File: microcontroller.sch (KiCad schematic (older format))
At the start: 52 parts, among them J3 FH12A-10S-0.5SH55, J4 , J5 Conn_ARM_JTAG_SWD_20, J6 26642801RP2, SW0 SW_Push, SW1 SW_Push, SW2 SW_Push, SW3 SW_Push, SW6 SW_Push, U7 EFM32GG942F1024

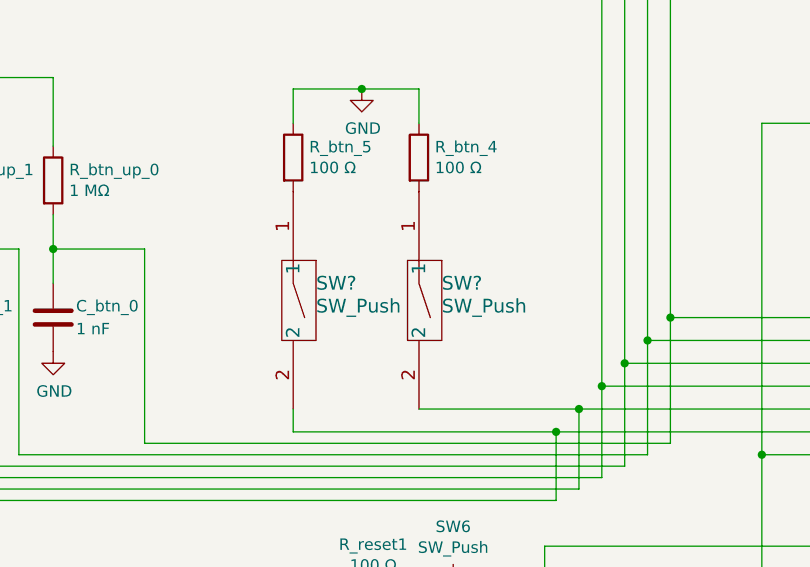
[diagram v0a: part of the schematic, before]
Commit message: Add led footprint
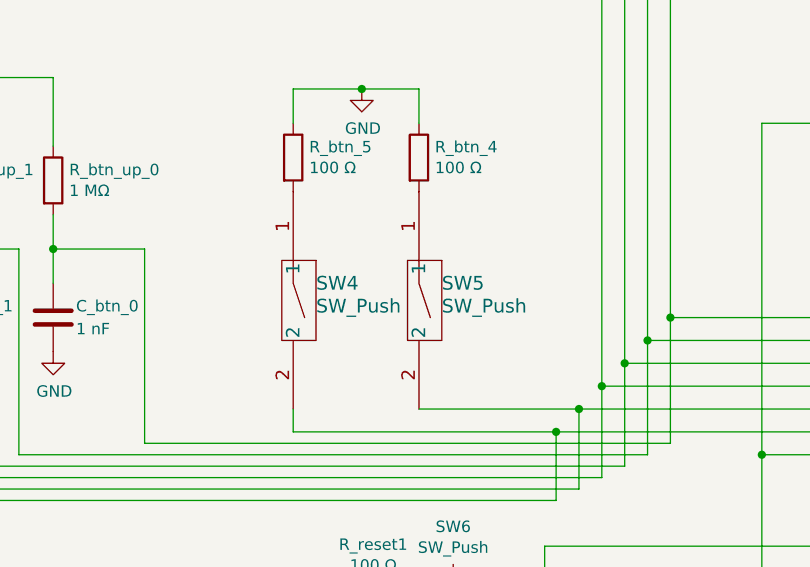
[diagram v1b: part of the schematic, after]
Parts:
- D1, D2: footprint (none) -> LED_SMD:LED_0805_2012Metric_Pad1.15x1.40mm_HandSolder
- gave numbers to parts that had none: 2
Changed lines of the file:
@@
 F 0 "D1" V 2000 4200 50  0000 C CNN
 F 1 "LED1" V 1900 4200 50  0000 C CNN
-F 2 "" H 2000 4050 50  0001 C CNN
+F 2 "LED_SMD:LED_0805_2012Metric_Pad1.15x1.40mm_HandSolder" H 2000 4050 50  0001 C CNN
 F 3 "~" H 2000 4050 50  0001 C CNN
 	1    2000 4050
@@
 F 0 "D2" V 2400 4200 50  0000 C CNN
 F 1 "LED2" V 2300 4200 50  0000 C CNN
-F 2 "" H 2400 4050 50  0001 C CNN
+F 2 "LED_SMD:LED_0805_2012Metric_Pad1.15x1.40mm_HandSolder" H 2400 4050 50  0001 C CNN
 F 3 "~" H 2400 4050 50  0001 C CNN
 	1    2400 4050
@@
 $EndComp
 $Comp
-L button:FSMSMTR SW?
+L button:FSMSMTR SW5
 U 1 1 5DEB7741
 P 1150 1450
-F 0 "SW?" V 1800 1550 60  0000 L CNN
+F 0 "SW5" V 1800 1550 60  0000 L CNN
 F 1 "SW_Push" V 1900 1550 60  0000 L CNN
 F 2 "SWITCH_FSMSMTR" H 1900 1590 60  0001 C CNN
@@
 $EndComp
 $Comp
-L button:FSMSMTR SW?
+L button:FSMSMTR SW4
 U 1 1 5DEB7747
 P 600 1450
-F 0 "SW?" V 1250 1550 60  0000 L CNN
+F 0 "SW4" V 1250 1550 60  0000 L CNN
 F 1 "SW_Push" V 1350 1550 60  0000 L CNN
 F 2 "SWITCH_FSMSMTR" H 1350 1590 60  0001 C CNN

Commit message: Minor unrelated fixes
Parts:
- Crystal_GND24: footprint (none) -> Crystal:Crystal_SMD_Abracon_ABM8G-4Pin_3.2x2.5mm
- SW6: footprint (none) -> Button_Switch_SMD:SW_SPST_FSMSM
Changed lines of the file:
@@
 F 0 "Crystal_GND24" H 2225 6300 50  0000 L CNN
 F 1 "48MHz" H 2225 6225 50  0000 L CNN
-F 2 "" H 2100 6100 50  0001 C CNN
+F 2 "Crystal:Crystal_SMD_Abracon_ABM8G-4Pin_3.2x2.5mm" H 2100 6100 50  0001 C CNN
 F 3 "" H 2100 6100 50  0001 C CNN
 	1    2100 6100
@@
 F 0 "SW6" H 1300 3735 50  0000 C CNN
 F 1 "SW_Push" H 1300 3644 50  0000 C CNN
-F 2 "" H 1300 3650 50  0001 C CNN
+F 2 "Button_Switch_SMD:SW_SPST_FSMSM" H 1300 3650 50  0001 C CNN
 F 3 "~" H 1300 3650 50  0001 C CNN
 	1    1300 3450

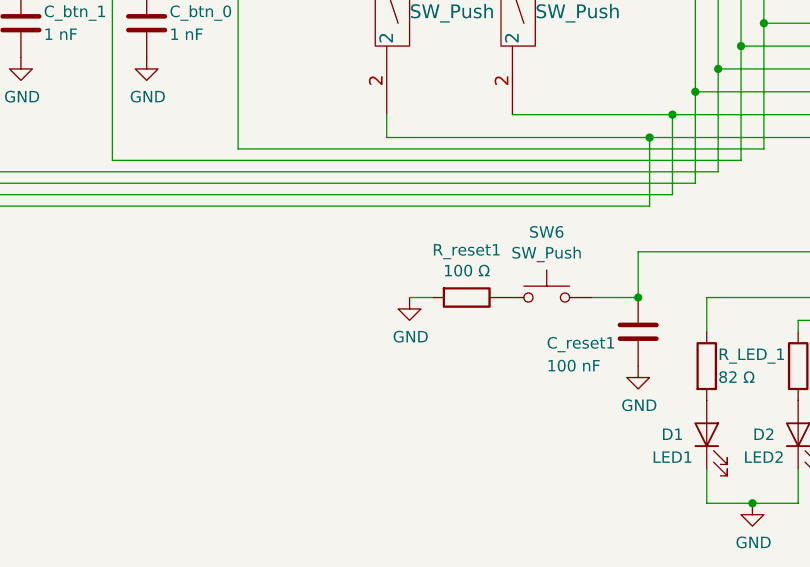
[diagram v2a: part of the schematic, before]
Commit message: Add efm and button footprints
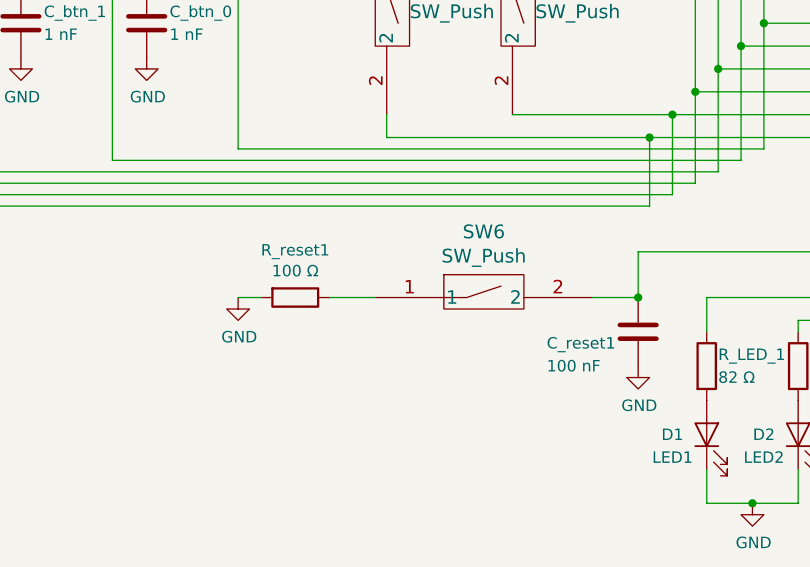
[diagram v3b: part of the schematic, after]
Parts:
- removed SW6: SW_Push, Button_Switch_SMD:SW_SPST_FSMSM, symbol Switch:SW_Push
- added SW6: SW_Push, button:FSMSMTR, symbol button:FSMSMTR
- Crystal_GND24: footprint Crystal:Crystal_SMD_Abracon_ABM8G-4Pin_3.2x2.5mm -> (none)
- SW0, SW1, SW2, SW3, SW4, SW5: footprint SWITCH_FSMSMTR -> button:FSMSMTR
- U7: footprint QFP64_10X10 -> efm32:EFM32GG942F1024
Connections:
- net at C_reset1.1, J5.15 (~SRST~), U7.20 (RESETN): now also SW6.2
- net at R_reset1.1: now also SW6.1
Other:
- moved on the sheet: R_reset1
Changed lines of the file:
@@
 F 0 "U7" H 5550 2650 60  0000 C CNN
 F 1 "EFM32GG942F1024" H 5550 2550 60  0000 C CNN
-F 2 "QFP64_10X10" H 5550 2490 60  0001 C CNN
+F 2 "efm32:EFM32GG942F1024" H 5550 2490 60  0001 C CNN
 F 3 "" H 4450 2250 60  0000 C CNN
 	1    4450 2250
@@
 F 0 "Crystal_GND24" H 2225 6300 50  0000 L CNN
 F 1 "48MHz" H 2225 6225 50  0000 L CNN
-F 2 "Crystal:Crystal_SMD_Abracon_ABM8G-4Pin_3.2x2.5mm" H 2100 6100 50  0001 C CNN
+F 2 "" H 2100 6100 50  0001 C CNN
 F 3 "" H 2100 6100 50  0001 C CNN
 	1    2100 6100
@@
 L Device:R R_reset1
 U 1 1 5D97B808
-P 950 3450
-F 0 "R_reset1" V 743 3450 50  0000 C CNN
-F 1 "100 Ω" V 834 3450 50  0000 C CNN
-F 2 "Resistor_SMD:R_1206_3216Metric_Pad1.42x1.75mm_HandSolder" V 880 3450 50  0001 C CNN
-F 3 "~" H 950 3450 50  0001 C CNN
-	1    950  3450
+P 200 3450
+F 0 "R_reset1" V -7  3450 50  0000 C CNN
+F 1 "100 Ω" V 84  3450 50  0000 C CNN
+F 2 "Resistor_SMD:R_1206_3216Metric_Pad1.42x1.75mm_HandSolder" V 130 3450 50  0001 C CNN
+F 3 "~" H 200 3450 50  0001 C CNN
+	1    200  3450
 	0    1    1    0
 $EndComp
@@
 L power:GND #PWR0152
 U 1 1 5D97C895
-P 700 3450
-F 0 "#PWR0152" H 700 3200 50  0001 C CNN
-F 1 "GND" H 705 3277 50  0000 C CNN
-F 2 "" H 700 3450 50  0001 C CNN
-F 3 "" H 700 3450 50  0001 C CNN
-	1    700  3450
-	1    0    0    -1
-$EndComp
-Wire Wire Line
-	800  3450 700  3450
+P -50 3450
+F 0 "#PWR0152" H -50 3200 50  0001 C CNN
+F 1 "GND" H -45 3277 50  0000 C CNN
+F 2 "" H -50 3450 50  0001 C CNN
+F 3 "" H -50 3450 50  0001 C CNN
+	1    -50  3450
+	1    0    0    -1
+$EndComp
+Wire Wire Line
+	50   3450 -50  3450
 $Comp
 L Device:C C_reset1
@@
 	-2650 1200 -2100 1200
 Connection ~ -2100 1200
-$Comp
-L Switch:SW_Push SW6
-U 1 1 5D97A033
-P 1300 3450
-F 0 "SW6" H 1300 3735 50  0000 C CNN
-F 1 "SW_Push" H 1300 3644 50  0000 C CNN
-F 2 "Button_Switch_SMD:SW_SPST_FSMSM" H 1300 3650 50  0001 C CNN
-F 3 "~" H 1300 3650 50  0001 C CNN
-	1    1300 3450
-	1    0    0    -1
-$EndComp
 Wire Wire Line
 	-2100 1800 -2100 1950
@@
 F 0 "SW0" V 2922 -1322 60  0000 L CNN
 F 1 "SW_Push" V 3028 -1322 60  0000 L CNN
-F 2 "SWITCH_FSMSMTR" H 3000 -1310 60  0001 C CNN
+F 2 "button:FSMSMTR" H 3000 -1310 60  0001 C CNN
 F 3 "" H 2500 -1450 60  0000 C CNN
 	1    2250 -1450
@@
 F 0 "SW1" V 2350 -1350 60  0000 L CNN
 F 1 "SW_Push" V 2450 -1350 60  0000 L CNN
-F 2 "SWITCH_FSMSMTR" H 2450 -1310 60  0001 C CNN
+F 2 "button:FSMSMTR" H 2450 -1310 60  0001 C CNN
 F 3 "" H 1950 -1450 60  0000 C CNN
 	1    1700 -1450
@@
 F 0 "SW2" V 1800 -1350 60  0000 L CNN
 F 1 "SW_Push" V 1900 -1350 60  0000 L CNN
-F 2 "SWITCH_FSMSMTR" H 1900 -1310 60  0001 C CNN
+F 2 "button:FSMSMTR" H 1900 -1310 60  0001 C CNN
 F 3 "" H 1400 -1450 60  0000 C CNN
 	1    1150 -1450
@@
 F 0 "SW3" V 1250 -1350 60  0000 L CNN
 F 1 "SW_Push" V 1350 -1350 60  0000 L CNN
-F 2 "SWITCH_FSMSMTR" H 1350 -1310 60  0001 C CNN
+F 2 "button:FSMSMTR" H 1350 -1310 60  0001 C CNN
 F 3 "" H 850 -1450 60  0000 C CNN
 	1    600  -1450
@@
 F 0 "SW5" V 1800 1550 60  0000 L CNN
 F 1 "SW_Push" V 1900 1550 60  0000 L CNN
-F 2 "SWITCH_FSMSMTR" H 1900 1590 60  0001 C CNN
+F 2 "button:FSMSMTR" H 1900 1590 60  0001 C CNN
 F 3 "" H 1400 1450 60  0000 C CNN
 	1    1150 1450
@@
 F 0 "SW4" V 1250 1550 60  0000 L CNN
 F 1 "SW_Push" V 1350 1550 60  0000 L CNN
-F 2 "SWITCH_FSMSMTR" H 1350 1590 60  0001 C CNN
+F 2 "button:FSMSMTR" H 1350 1590 60  0001 C CNN
 F 3 "" H 850 1450 60  0000 C CNN
 	1    600  1450
@@
 Wire Wire Line
 	1950 -50  1950 2550
+$Comp
+L button:FSMSMTR SW6
+U 1 1 5D94F3D9
+P 300 3450
+F 0 "SW6" H 1025 3737 60  0000 C CNN
+F 1 "SW_Push" H 1025 3631 60  0000 C CNN
+F 2 "button:FSMSMTR" H 1050 3590 60  0001 C CNN
+F 3 "" H 550 3450 60  0000 C CNN
+	1    300  3450
+	1    0    0    -1
+$EndComp
+Wire Wire Line
+	550  3450 350  3450
 $EndSCHEMATC

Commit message: Minor fixes
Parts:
- Crystal_GND24: footprint (none) -> Crystal:Crystal_SMD_Abracon_ABM8G-4Pin_3.2x2.5mm
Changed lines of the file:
@@
 F 0 "Crystal_GND24" H 2225 6300 50  0000 L CNN
 F 1 "48MHz" H 2225 6225 50  0000 L CNN
-F 2 "" H 2100 6100 50  0001 C CNN
+F 2 "Crystal:Crystal_SMD_Abracon_ABM8G-4Pin_3.2x2.5mm" H 2100 6100 50  0001 C CNN
 F 3 "" H 2100 6100 50  0001 C CNN
 	1    2100 6100

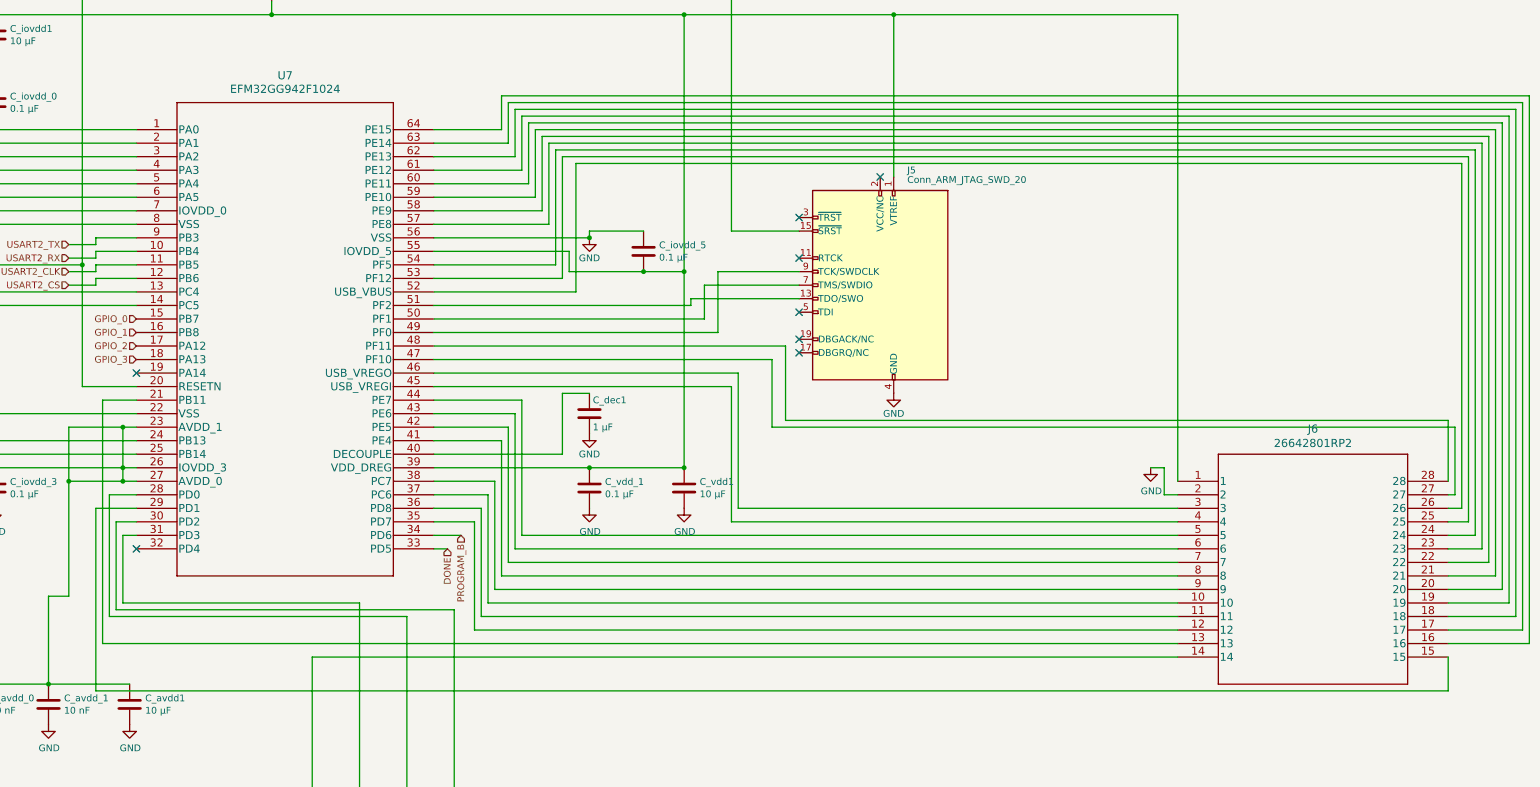
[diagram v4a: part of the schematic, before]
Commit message: Fix pin headers
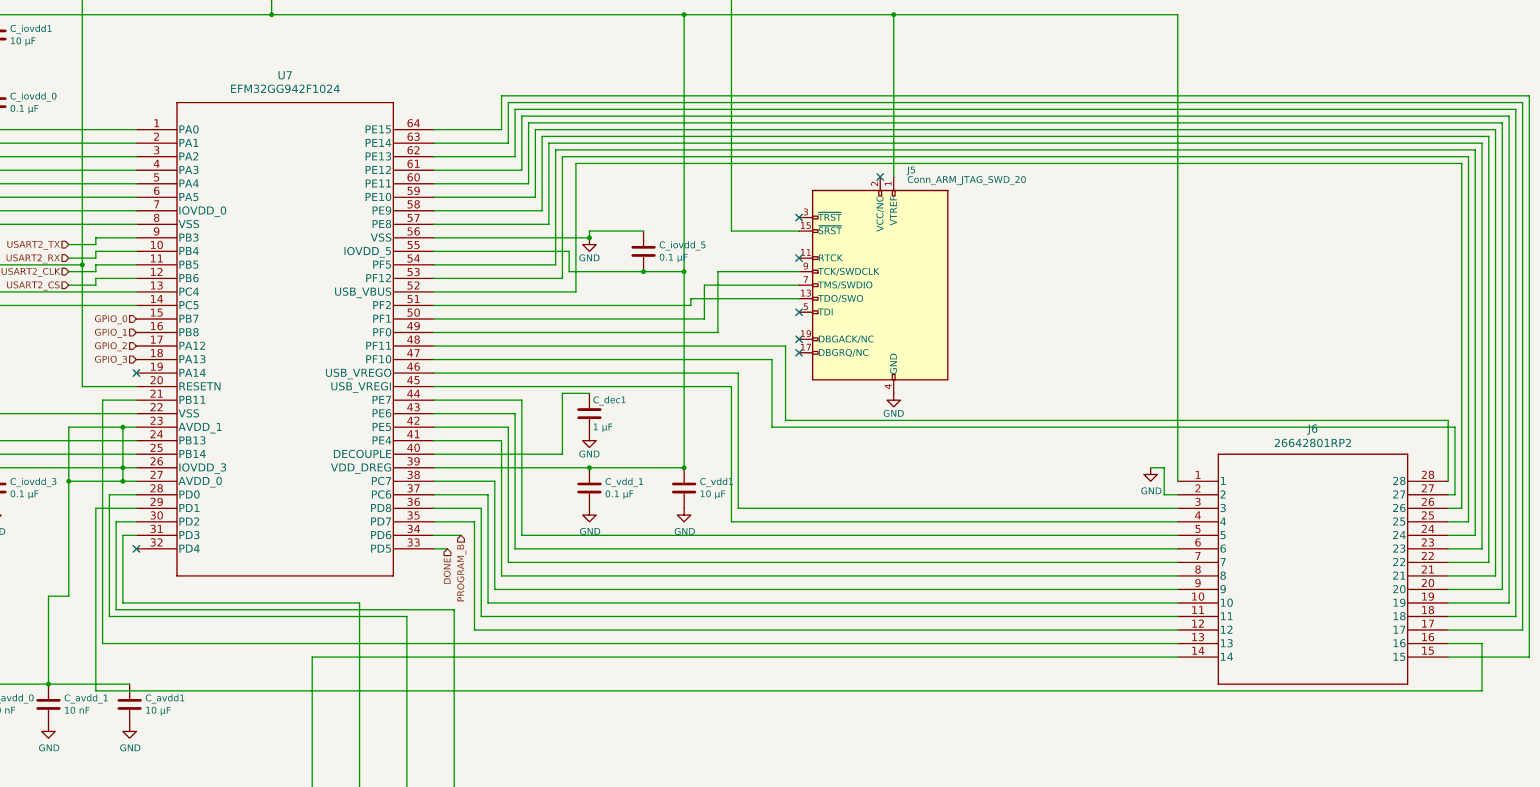
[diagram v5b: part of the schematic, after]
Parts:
- J6: footprint CON28_2X14_HDR_2664 -> Connector_PinHeader_2.54mm:PinHeader_2x14_P2.54mm_Vertical
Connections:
- net at U7.29 (PD1): now also J6.16; no longer J6.15
- net at U7.64 (PE15): now also J6.15; no longer J6.16
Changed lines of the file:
@@
 F 0 "J6" H 13150 5237 60  0000 C CNN
 F 1 "26642801RP2" H 13150 5131 60  0000 C CNN
-F 2 "CON28_2X14_HDR_2664" H 13150 5090 60  0001 C CNN
+F 2 "Connector_PinHeader_2.54mm:PinHeader_2x14_P2.54mm_Vertical" H 13150 5090 60  0001 C CNN
 F 3 "" H 12150 4850 60  0000 C CNN
 	1    12150 4850
@@
 	7150 2000 14750 2000
 Wire Wire Line
-	14750 2000 14750 6050
-Wire Wire Line
-	14750 6050 14150 6050
-Wire Wire Line
 	4450 4250 4200 4250
 Wire Wire Line
@@
 Wire Wire Line
 	4150 5050 4150 6400
-Wire Wire Line
-	4150 6400 14150 6400
-Wire Wire Line
-	14150 6400 14150 6150
 NoConn ~ 4450 5350
 NoConn ~ 4450 4050
@@
 Wire Wire Line
 	550  3450 350  3450
+Wire Wire Line
+	14150 6150 14750 6150
+Wire Wire Line
+	14750 2000 14750 6150
+Wire Wire Line
+	14400 6400 14400 6050
+Wire Wire Line
+	14400 6050 14150 6050
+Wire Wire Line
+	4150 6400 14400 6400
 $EndSCHEMATC

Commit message: Fix all footprints
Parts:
- J3, J4: footprint CONN10_1X10_DRC_FFC -> Local:FH12A-10S-0.5SH55
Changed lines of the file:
@@
 F 0 "J4" V 3750 9200 60  0000 C CNN
 F 1 " " V 4200 9050 60  0000 C CNN
-F 2 "CONN10_1X10_DRC_FFC" H 4000 8990 60  0001 C CNN
+F 2 "Local:FH12A-10S-0.5SH55" H 4000 8990 60  0001 C CNN
 F 3 "" H 4000 9050 60  0000 C CNN
 	2    4000 9050
@@
 F 0 "J4" V 4092 9148 60  0000 L CNN
 F 1 " " V 4198 9148 60  0000 L CNN
-F 2 "CONN10_1X10_DRC_FFC" H 4350 8990 60  0001 C CNN
+F 2 "Local:FH12A-10S-0.5SH55" H 4350 8990 60  0001 C CNN
 F 3 "" H 4350 9050 60  0000 C CNN
 	3    4350 9050
@@
 F 0 "J4" V 4442 9148 60  0000 L CNN
 F 1 " " V 4548 9148 60  0000 L CNN
-F 2 "CONN10_1X10_DRC_FFC" H 4700 8990 60  0001 C CNN
+F 2 "Local:FH12A-10S-0.5SH55" H 4700 8990 60  0001 C CNN
 F 3 "" H 4700 9050 60  0000 C CNN
 	4    4700 9050
@@
 F 0 "J4" V 4792 9148 60  0000 L CNN
 F 1 " " V 4898 9148 60  0000 L CNN
-F 2 "CONN10_1X10_DRC_FFC" H 5050 8990 60  0001 C CNN
+F 2 "Local:FH12A-10S-0.5SH55" H 5050 8990 60  0001 C CNN
 F 3 "" H 5050 9050 60  0000 C CNN
 	5    5050 9050
@@
 F 0 "J4" V 5142 9148 60  0000 L CNN
 F 1 " " V 5248 9148 60  0000 L CNN
-F 2 "CONN10_1X10_DRC_FFC" H 5400 8990 60  0001 C CNN
+F 2 "Local:FH12A-10S-0.5SH55" H 5400 8990 60  0001 C CNN
 F 3 "" H 5400 9050 60  0000 C CNN
 	6    5400 9050
@@
 F 0 "J4" V 5492 9147 60  0000 L CNN
 F 1 " " V 5598 9147 60  0000 L CNN
-F 2 "CONN10_1X10_DRC_FFC" H 5750 8990 60  0001 C CNN
+F 2 "Local:FH12A-10S-0.5SH55" H 5750 8990 60  0001 C CNN
 F 3 "" H 5750 9050 60  0000 C CNN
 	7    5750 9050
@@
 F 0 "J4" V 5842 9147 60  0000 L CNN
 F 1 " " V 5948 9147 60  0000 L CNN
-F 2 "CONN10_1X10_DRC_FFC" H 6100 8990 60  0001 C CNN
+F 2 "Local:FH12A-10S-0.5SH55" H 6100 8990 60  0001 C CNN
 F 3 "" H 6100 9050 60  0000 C CNN
 	8    6100 9050
@@
 F 0 "J4" V 6163 9148 60  0000 L CNN
 F 1 " " V 6269 9148 60  0000 L CNN
-F 2 "CONN10_1X10_DRC_FFC" H 6450 8990 60  0001 C CNN
+F 2 "Local:FH12A-10S-0.5SH55" H 6450 8990 60  0001 C CNN
 F 3 "" H 6450 9050 60  0000 C CNN
 	9    6450 9050
@@
 F 0 "J4" V 6513 9148 60  0000 L CNN
 F 1 " " V 6619 9148 60  0000 L CNN
-F 2 "CONN10_1X10_DRC_FFC" H 6800 8990 60  0001 C CNN
+F 2 "Local:FH12A-10S-0.5SH55" H 6800 8990 60  0001 C CNN
 F 3 "" H 6800 9050 60  0000 C CNN
 	10   6800 9050
@@
 F 0 "J4" V 6863 9147 60  0000 L CNN
 F 1 " " V 6969 9147 60  0000 L CNN
-F 2 "CONN10_1X10_DRC_FFC" H 7150 8990 60  0001 C CNN
+F 2 "Local:FH12A-10S-0.5SH55" H 7150 8990 60  0001 C CNN
 F 3 "" H 7150 9050 60  0000 C CNN
 	11   7150 9050
@@
 F 0 "J3" V 3100 9250 60  0000 C CNN
 F 1 "FH12A-10S-0.5SH55" V 3050 10800 60  0000 C CNN
-F 2 "CONN10_1X10_DRC_FFC" H 3650 8990 60  0001 C CNN
+F 2 "Local:FH12A-10S-0.5SH55" H 3650 8990 60  0001 C CNN
 F 3 "" H 3650 9050 60  0000 C CNN
 	1    3650 9050
@@
 F 0 "J4" V 7250 9000 60  0000 R CNN
 F 1 " " V 7213 8988 60  0000 R CNN
-F 2 "CONN10_1X10_DRC_FFC" H 7500 8990 60  0001 C CNN
+F 2 "Local:FH12A-10S-0.5SH55" H 7500 8990 60  0001 C CNN
 F 3 "" H 7500 9050 60  0000 C CNN
 	12   7500 9050

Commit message: Add JTAG footprint
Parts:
- J5: footprint (none) -> Connector_PinHeader_2.54mm:PinHeader_2x10_P2.54mm_Vertical
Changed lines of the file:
@@
 F 0 "J5" H 9750 4250 50  0000 R CNN
 F 1 "Conn_ARM_JTAG_SWD_20" H 9750 4150 50  0000 R BNN
-F 2 "" H 10400 2350 50  0001 L TNN
+F 2 "Connector_PinHeader_2.54mm:PinHeader_2x10_P2.54mm_Vertical" H 10400 2350 50  0001 L TNN
 F 3 "" V 9600 2150 50  0001 C CNN
 	1    9950 3400
